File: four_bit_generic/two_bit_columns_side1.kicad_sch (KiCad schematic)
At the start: 86 parts

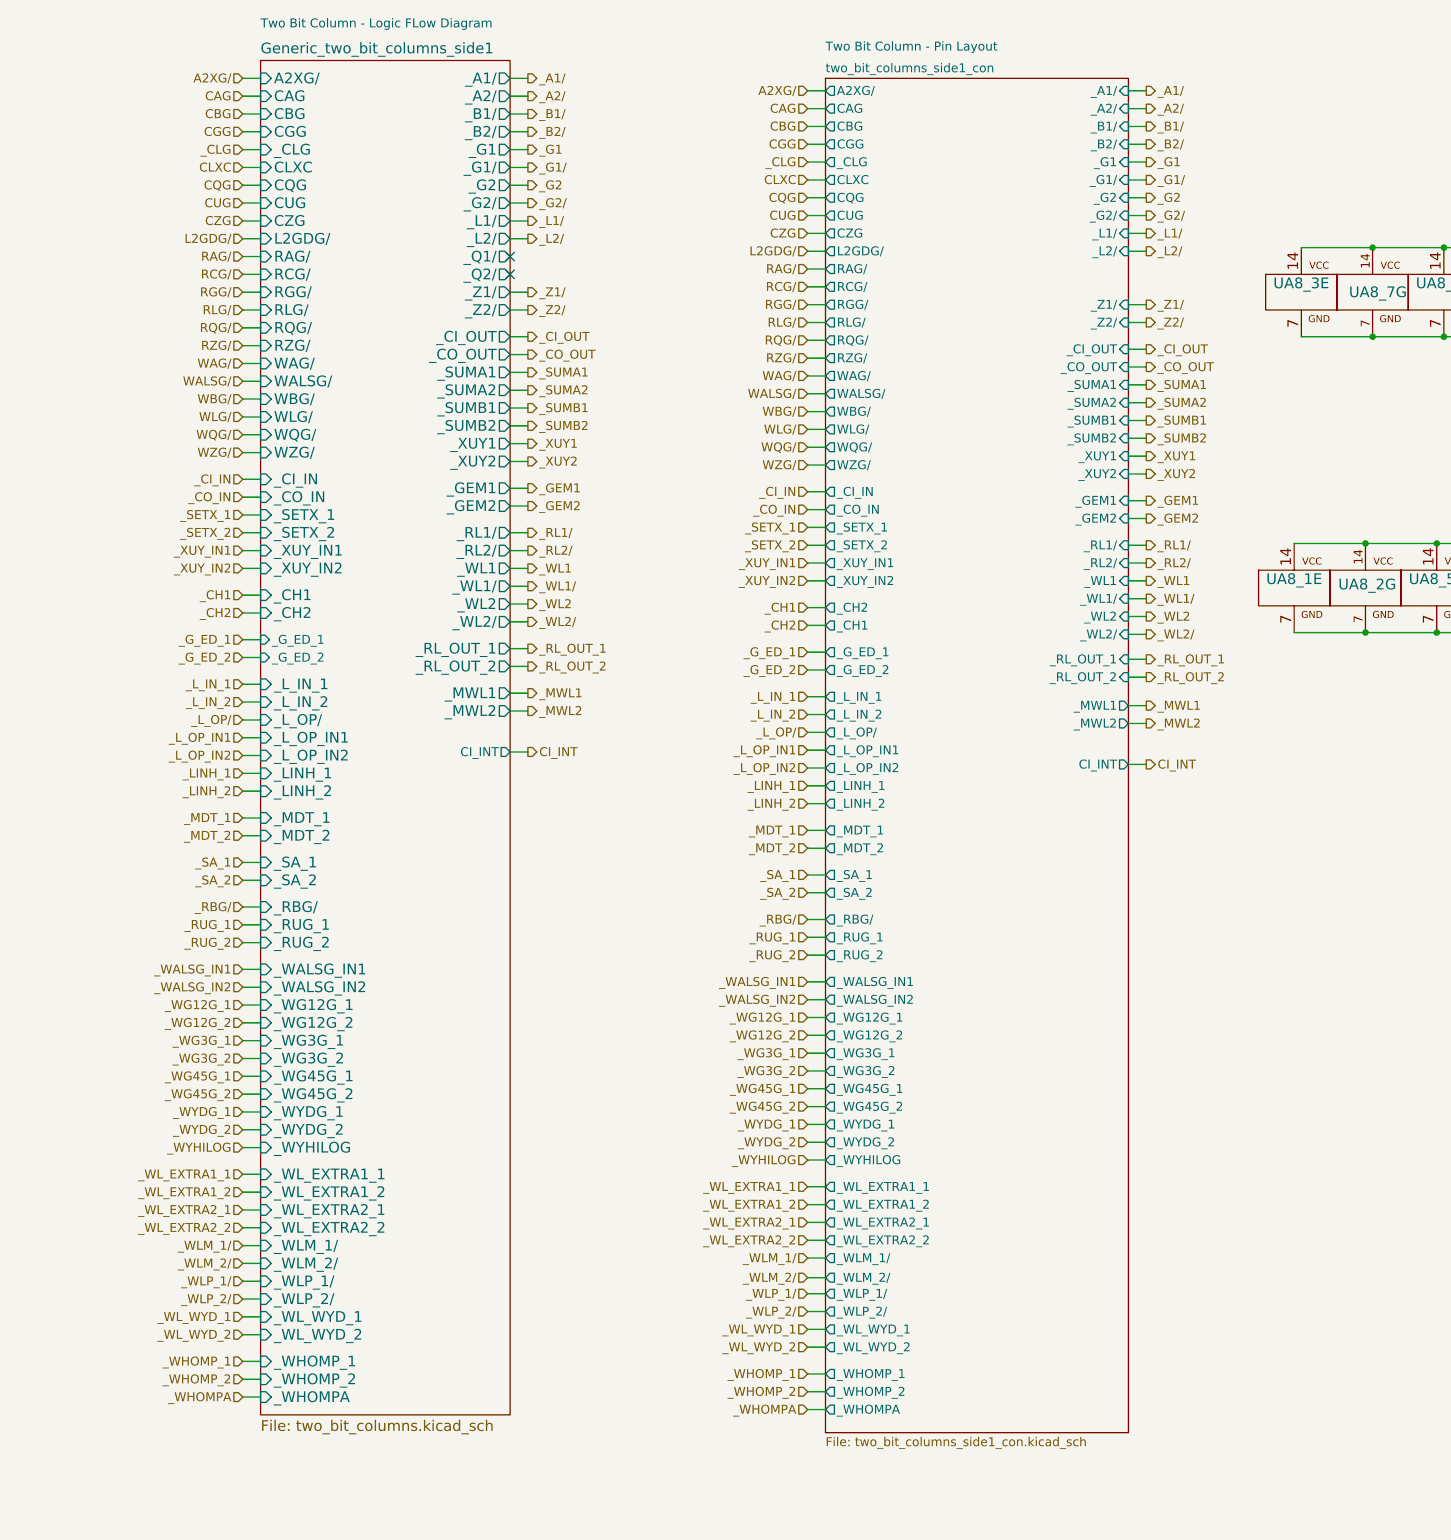
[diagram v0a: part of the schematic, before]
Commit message: Generic  4 Bit Adder schematic + pcb
PCB and schematic updates
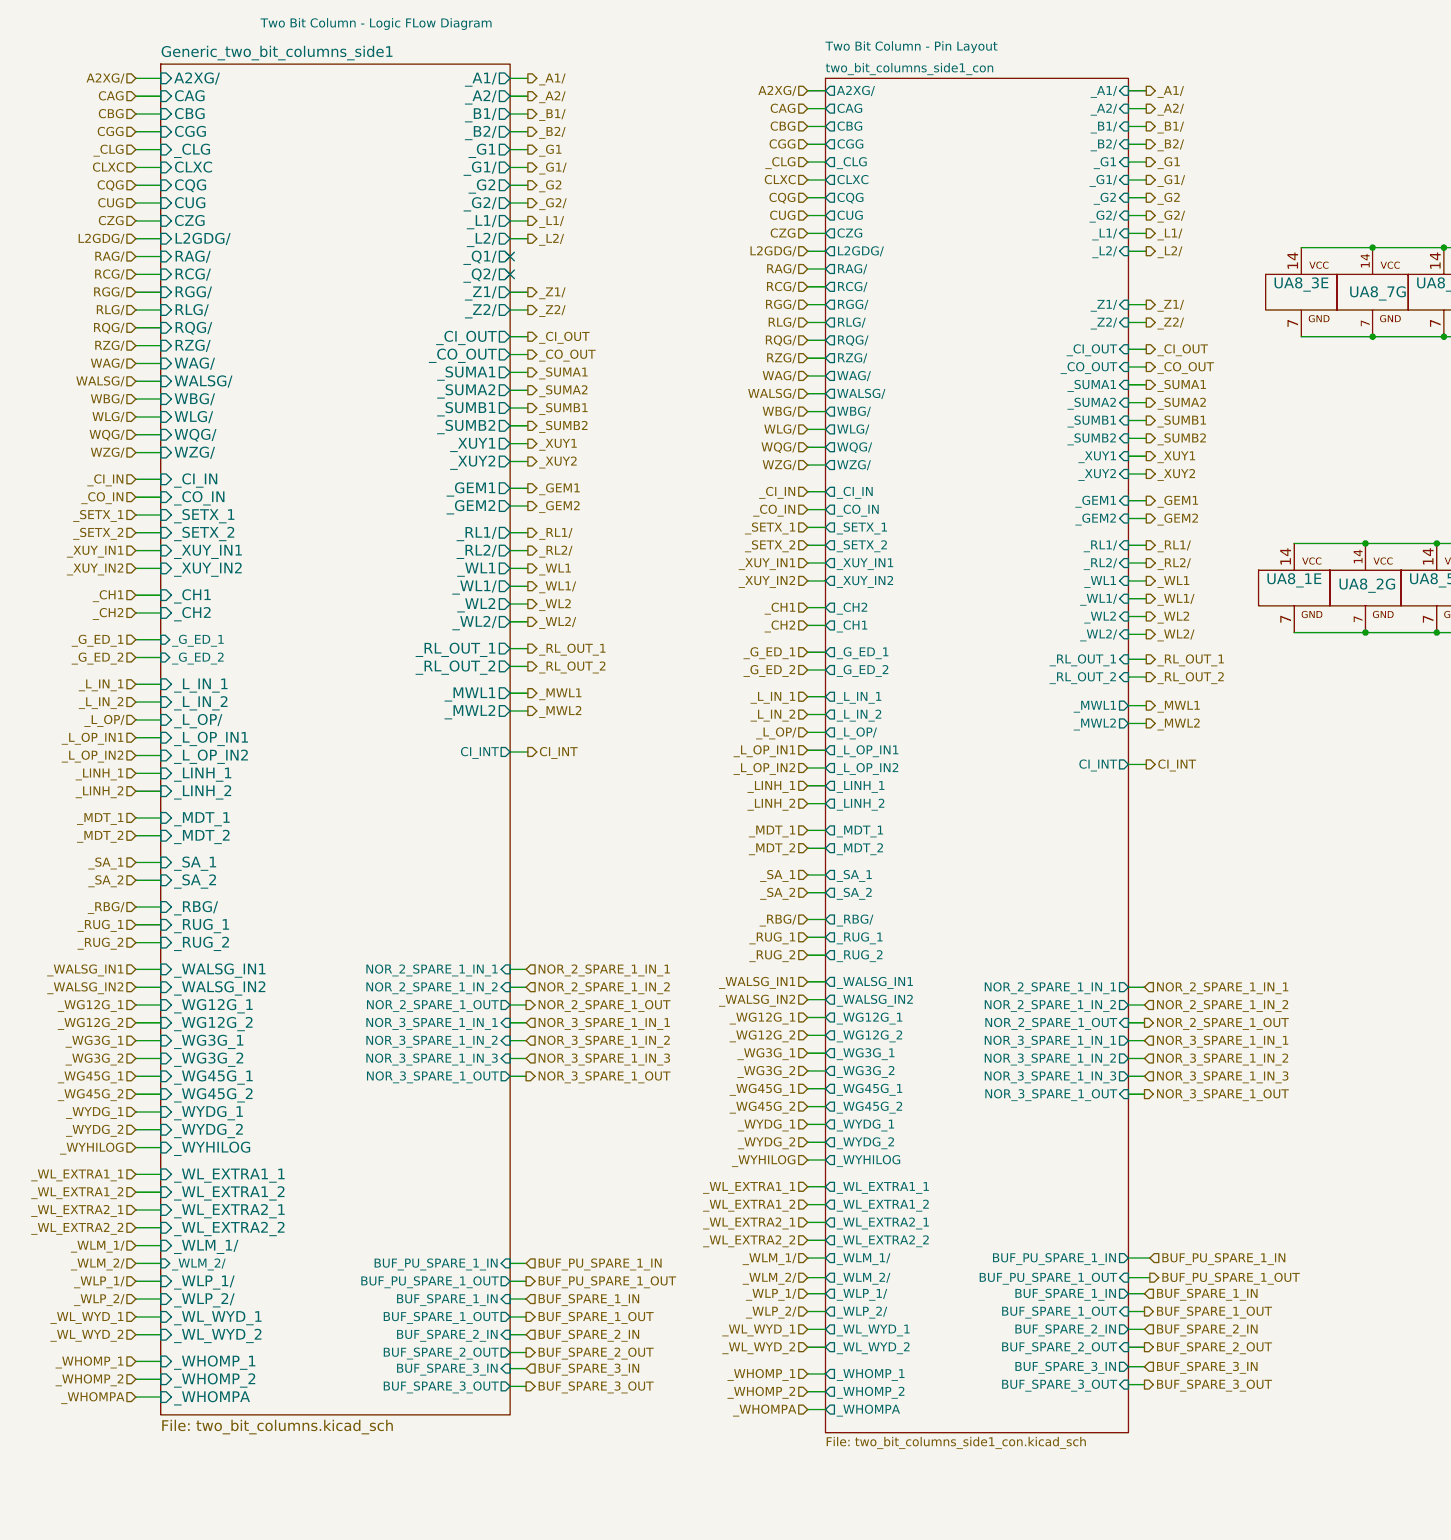
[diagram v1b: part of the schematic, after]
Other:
- sheet Generic_two_bit_columns_side1 ports: added BUF_PU_SPARE_1_IN, BUF_PU_SPARE_1_OUT, BUF_SPARE_1_IN, BUF_SPARE_1_OUT, BUF_SPARE_2_IN, BUF_SPARE_2_OUT, BUF_SPARE_3_IN, BUF_SPARE_3_OUT, NOR_2_SPARE_1_IN_1, NOR_2_SPARE_1_IN_2, NOR_2_SPARE_1_OUT, NOR_3_SPARE_1_IN_1, NOR_3_SPARE_1_IN_2, NOR_3_SPARE_1_IN_3, NOR_3_SPARE_1_OUT, _WLM_2/; removed _WLM_2/
- sheet two_bit_columns_side1_con ports: added BUF_PU_SPARE_1_IN, BUF_PU_SPARE_1_OUT, BUF_SPARE_1_IN, BUF_SPARE_1_OUT, BUF_SPARE_2_IN, BUF_SPARE_2_OUT, BUF_SPARE_3_IN, BUF_SPARE_3_OUT, NOR_2_SPARE_1_IN_1, NOR_2_SPARE_1_IN_2, NOR_2_SPARE_1_OUT, NOR_3_SPARE_1_IN_1, NOR_3_SPARE_1_IN_2, NOR_3_SPARE_1_IN_3, NOR_3_SPARE_1_OUT; removed none
